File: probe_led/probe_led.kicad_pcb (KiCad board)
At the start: 2 copper layers, 60 x 7 mm, 39 parts

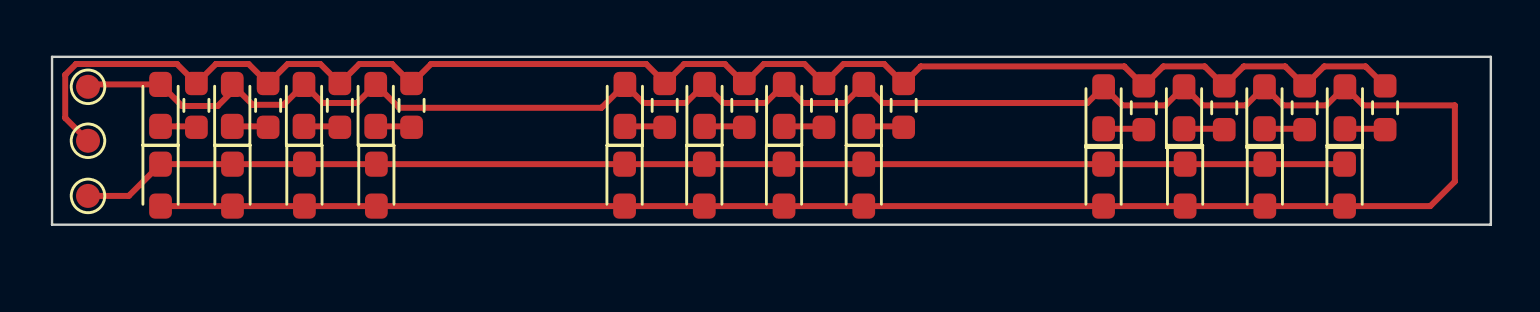
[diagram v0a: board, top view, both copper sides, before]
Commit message: - add led pcb
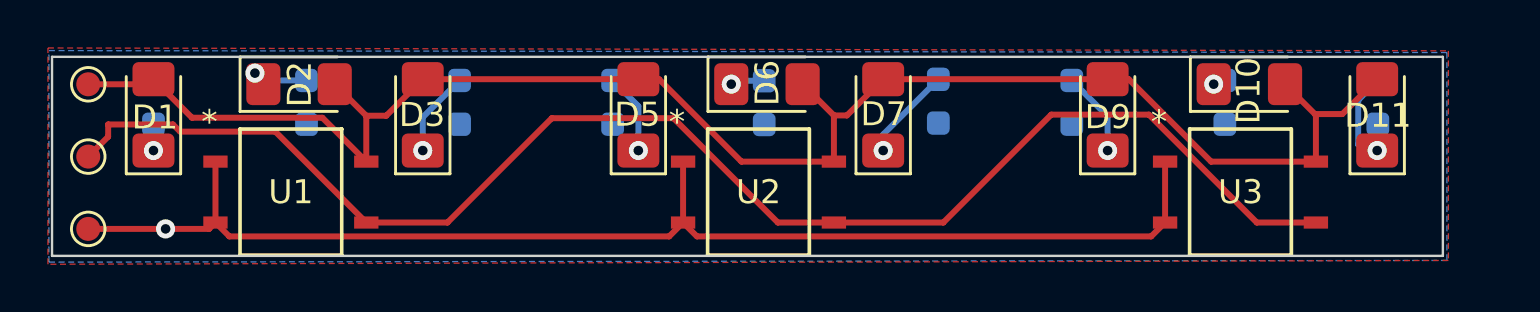
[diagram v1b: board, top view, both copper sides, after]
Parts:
- removed D12, D4, D8, IR10, IR11, IR12, IR2, IR3, IR4, IR5, IR6, IR7, IR8, IR9: LED, LED_SMD:LED_0603_1608Metric_Pad1.05x0.95mm_HandSolder
- removed the IR1 at (104.5, 82.0)
- removed R12, R4, R8: R, Resistor_SMD:R_0603_1608Metric_Pad0.98x0.95mm_HandSolder
- added U1: IRM-H638T_TR2, IRM-H638T:IRM-H638T&slash_TR2_EVE-L, F.Cu at (110.0, 82.3)
- added U2: IRM-H638T_TR2, IRM-H638T:IRM-H638T&slash_TR2_EVE-L, F.Cu at (129.5, 82.3)
- added U3: IRM-H638T_TR2, IRM-H638T:IRM-H638T&slash_TR2_EVE-L, F.Cu at (149.6, 82.3)
- D1, D10, D11, D2, D3, D5, D6, D7, D9: footprint LED_SMD:LED_0603_1608Metric_Pad1.05x0.95mm_HandSolder -> LED_SMD:LED_1206_3216Metric_Pad1.42x1.75mm_HandSolder
- R1, R10, R11, R2, R3, R5, R6, R7, R9: moved to B.Cu
- moved R3 4.99 mm to (117.0, 78.6), turned to -90 degrees
- moved D3 4.97 mm to (115.5, 79.1)
- moved R7 4.77 mm to (137.0, 78.5), turned to -90 degrees
- moved D11 4.71 mm to (155.3, 79.1)
- moved D7 4.15 mm to (134.7, 79.1)
- moved GND1 3.68 mm to (101.5, 83.9)
- moved R11 3.06 mm to (155.3, 78.6), turned to -90 degrees
- moved R9 3.01 mm to (142.5, 78.6), turned to -90 degrees
- moved D2 2.92 mm to (110.3, 77.8), turned to 0 degrees
- moved D10 2.90 mm to (149.9, 77.8), turned to 0 degrees
- moved D6 2.75 mm to (129.8, 77.8), turned to 0 degrees
- moved R5 2.17 mm to (123.4, 78.6), turned to -90 degrees
- moved R1 1.79 mm to (104.2, 78.6)
- moved IR1 1.64 mm to (101.5, 80.9)
- moved R2 1.61 mm to (110.6, 78.6), turned to -90 degrees
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- renumbered 5V to 5V1, GND to GND1, IR to IR1
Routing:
- net +5V: track 122.7 -> 71.3 mm
- net GND: track 66.1 -> 53.6 mm, vias 0 -> 1
- net Net-(IR1-Pad1): track 52.9 -> 61.1 mm
- net Net-(D11-Pad1): track 1.69 -> 4.12 mm, vias 0 -> 1
- net Net-(D7-Pad1): track 1.68 -> 3.92 mm, vias 0 -> 1
- net Net-(D3-Pad1): track 1.51 -> 3.56 mm, vias 0 -> 1
- net Net-(D9-Pad1): track 1.69 -> 3.54 mm, vias 0 -> 1
- net Net-(D12-Pad1): track 1.69 -> 0.00 mm
- net Net-(D5-Pad1): track 1.68 -> 3.37 mm, vias 0 -> 1
- net Net-(D8-Pad1): track 1.68 -> 0.00 mm
- net Net-(D4-Pad1): track 1.51 -> 0.00 mm
- net Net-(D10-Pad1): track 1.69 -> 0.53 mm, vias 0 -> 1
- net Net-(D2-Pad1): track 1.51 -> 2.28 mm, vias 0 -> 1
- net Net-(D1-Pad1): track 1.51 -> 1.10 mm, vias 0 -> 1
- net Net-(D6-Pad1): track 1.68 -> 1.43 mm, vias 0 -> 1
- added copper zone on F.Cu, net +5V
- added copper zone on B.Cu, net GND
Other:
- board size 60 x 7 mm -> 58 x 8.3 mm

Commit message: - add new power version
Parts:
- removed 5V1: 5V, TestPoint:TestPoint_Pad_D1.0mm
- added 5V: 5V, TestPoint:TestPoint_Pad_D1.0mm, F.Cu at (101.5, 77.7)
- added LED-: GND, TestPoint:TestPoint_Pad_D1.0mm, F.Cu at (101.5, 79.7)
- moved IR_D 0.95 mm to (101.5, 81.8)
- renumbered GND1 to IR-, IR1 to IR_D
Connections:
- net +5V renamed Net-(5V-Pad1)
- IR- pad 1: GND -> Net-(IR--Pad1)
- R1 pad 2: GND -> Net-(LED--Pad1)
- R10 pad 2: GND -> Net-(LED--Pad1)
- R11 pad 2: GND -> Net-(LED--Pad1)
- R2 pad 2: GND -> Net-(LED--Pad1)
- R3 pad 2: GND -> Net-(LED--Pad1)
- R5 pad 2: GND -> Net-(LED--Pad1)
- R6 pad 2: GND -> Net-(LED--Pad1)
- R7 pad 2: GND -> Net-(LED--Pad1)
- R9 pad 2: GND -> Net-(LED--Pad1)
- U1 pad 1: GND -> Net-(IR--Pad1)
- U1 pad 2: GND -> Net-(IR--Pad1)
- U2 pad 1: GND -> Net-(IR--Pad1)
- U2 pad 2: GND -> Net-(IR--Pad1)
- U3 pad 1: GND -> Net-(IR--Pad1)
- U3 pad 2: GND -> Net-(IR--Pad1)
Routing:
- net Net-(LED--Pad1): track 0.00 -> 75.3 mm, vias 0 -> 1
- net Net-(IR--Pad1): track 0.00 -> 53.6 mm
- net GND: track 53.6 -> 0.00 mm, vias 1 -> 0
- added copper zone on B.Cu, net Net-(LED--Pad1)
- removed copper zone on B.Cu, net GND

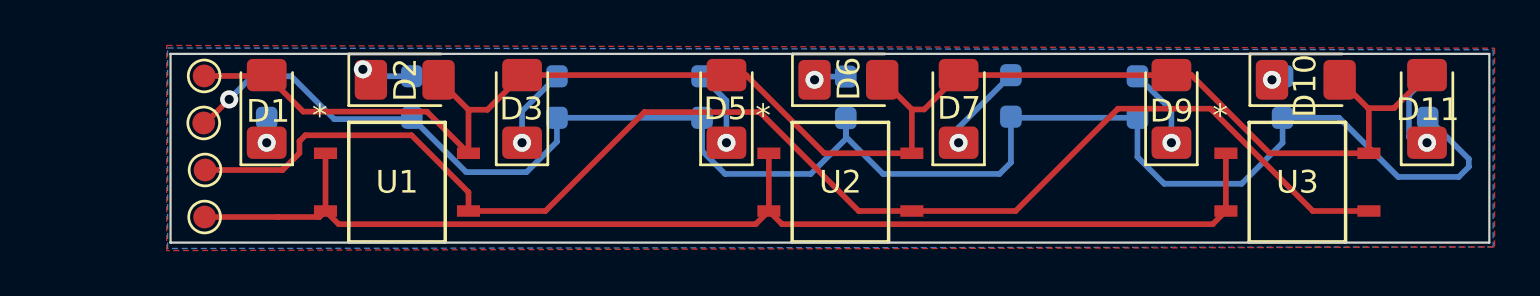
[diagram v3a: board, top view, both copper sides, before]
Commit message: -add new size led
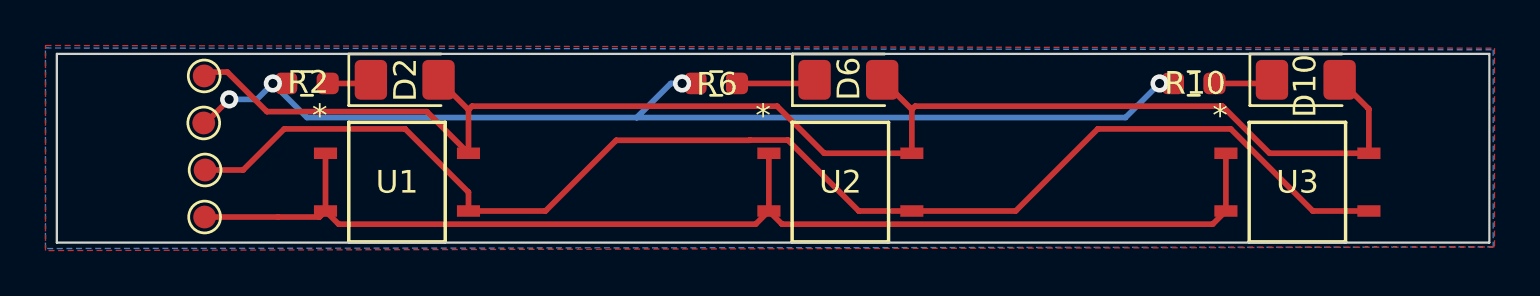
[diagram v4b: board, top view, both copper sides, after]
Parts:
- removed D1, D11, D3, D5, D7, D9: LED, LED_SMD:LED_1206_3216Metric_Pad1.42x1.75mm_HandSolder
- removed R1, R11, R3, R5, R7, R9: R, Resistor_SMD:R_0603_1608Metric_Pad0.98x0.95mm_HandSolder
- R10, R2, R6: moved to F.Cu
- moved R6 5.73 mm to (124.0, 78.0), turned to 180 degrees
- moved R2 4.65 mm to (106.0, 78.0), turned to 180 degrees
- moved R10 3.95 mm to (145.0, 78.0), turned to 180 degrees
- renumbered 5V to 5V1, IR- to IR-1, IR_D to IR_D1, LED- to LED-1
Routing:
- net Net-(LED-1-Pad1): track 75.3 -> 48.4 mm, vias 1 -> 4
- net Net-(D10-A): track 71.6 -> 65.9 mm
- net Net-(D11-Pad1): track 4.12 -> 0.00 mm, vias 1 -> 0
- net Net-(D7-Pad1): track 3.92 -> 0.00 mm, vias 1 -> 0
- net Net-(D3-Pad1): track 3.56 -> 0.00 mm, vias 1 -> 0
- net Net-(D9-Pad1): track 3.54 -> 0.00 mm, vias 1 -> 0
- net Net-(D5-Pad1): track 3.37 -> 0.00 mm, vias 1 -> 0
- net Net-(D10-K): track 0.53 -> 2.60 mm, vias 1 -> 0
- net Net-(D6-K): track 1.43 -> 3.48 mm, vias 1 -> 0
- net Net-(IR_D1-Pad1): track 61.3 -> 59.5 mm
- net Net-(D1-Pad1): track 1.10 -> 0.00 mm, vias 1 -> 0
- net Net-(D2-K): track 2.28 -> 1.97 mm, vias 1 -> 0
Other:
- board size 58 x 8.3 mm -> 63 x 8.3 mm

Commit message: -add new version for transmitter
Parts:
- added REF**: FPC_4pin_0.5mm_fingers, Connector_FFC-FPC:FPC_4pin_0.5mm_fingers, F.Cu at (98.3, 102.5)
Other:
- board size 63 x 8.3 mm -> 60.2 x 68.5 mm
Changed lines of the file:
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@@
 		)
+	)
+	(footprint "Connector_FFC-FPC:FPC_4pin_0.5mm_fingers"
+		(layer "F.Cu")
+		(at 98.3 102.54)
+		(property "Reference" "REF**"
+			(at 0 -4 0)
+			(unlocked yes)
+			(layer "F.SilkS")
+			(effects
+				(font
+					(size 1 1)
+					(thickness 0.15)
+				)
+			)
+		)
+		(property "Value" "FPC_4pin_0.5mm_fingers"
+			(at 0 7 0)
+			(unlocked yes)
+			(layer "F.Fab")
+			(effects
+				(font
+					(size 1 1)
+					(thickness 0.15)
+				)
+			)
+		)
+		(property "Datasheet" ""
+			(at 0 0 0)
+			(unlocked yes)
+			(layer "F.Fab")
+			(hide yes)
+			(effects
+				(font
+					(size 1 1)
+					(thickness 0.15)
+				)
+			)
+		)
+		(property "Description" ""
+			(at 0 0 0)
+			(unlocked yes)
+			(layer "F.Fab")
+			(hide yes)
+			(effects
+				(font
+					(size 1 1)
+					(thickness 0.15)
+				)
+			)
+		)
+		(attr smd)
+		(fp_text user "${REFERENCE}"
+			(at 0 9 0)
+			(unlocked yes)
+			(layer "F.Fab")
+			(effects
+				(font
+					(size 1 1)
+					(thickness 0.15)
+				)
+			)
+		)
+		(pad "1" smd roundrect
+			(at 0 0)
+			(size 0.3 5)
+			(layers "F.Cu" "F.Mask" "F.Paste")
+			(roundrect_rratio 0.15)
+			(thermal_bridge_angle 45)
+			(teardrops
+				(best_length_ratio 0.5)
+				(max_length 1)
+				(best_width_ratio 1)
+				(max_width 2)
+				(curved_edges no)
+				(filter_ratio 0.9)
+				(enabled yes)
+				(allow_two_segments yes)
+				(prefer_zone_connections yes)
+			)
+		)
+		(pad "2" smd roundrect
+			(at 0.5 0)
+			(size 0.3 5)
+			(layers "F.Cu" "F.Mask" "F.Paste")
+			(roundrect_rratio 0.15)
+			(thermal_bridge_angle 45)
+		)
+		(pad "3" smd roundrect
+			(at 1 0)
+			(size 0.3 5)
+			(layers "F.Cu" "F.Mask" "F.Paste")
+			(roundrect_rratio 0.15)
+			(thermal_bridge_angle 45)
+		)
+		(pad "4" smd roundrect
+			(at 1.5 0)
+			(size 0.3 5)
+			(layers "F.Cu" "F.Mask" "F.Paste")
+			(roundrect_rratio 0.15)
+			(thermal_bridge_angle 45)
+		)
+		(embedded_fonts no)
 	)
 	(footprint "Resistor_SMD:R_0603_1608Metric_Pad0.98x0.95mm_HandSolder"
@@
 		)
 	)
-	(gr_rect
-		(start 95 76.7)
-		(end 158 85)
+	(gr_line
+		(start 100.32 36.61)
+		(end 100.32 76.7)
 		(stroke
 			(width 0.1)
-			(type solid)
-		)
-		(fill no)
+			(type default)
+		)
+		(layer "Edge.Cuts")
+	)
+	(gr_line
+		(start 97.81 36.61)
+		(end 100.32 36.61)
+		(stroke
+			(width 0.1)
+			(type default)
+		)
+		(layer "Edge.Cuts")
+	)
+	(gr_line
+		(start 97.78 76.68)
+		(end 97.81 36.61)
+		(stroke
+			(width 0.1)
+			(type default)
+		)
+		(layer "Edge.Cuts")
+	)
+	(gr_line
+		(start 157.99 84.99)
+		(end 100.3 85.03)
+		(stroke
+			(width 0.1)
+			(type default)
+		)
+		(layer "Edge.Cuts")
+	)
+	(gr_line
+		(start 100.3 85.03)
+		(end 100.25 105.08)
+		(stroke
+			(width 0.1)
+			(type default)
+		)
+		(layer "Edge.Cuts")
+	)
+	(gr_line
+		(start 100.32 76.7)
+		(end 157.99 76.65)
+		(stroke
+			(width 0.1)
+			(type default)
+		)
+		(layer "Edge.Cuts")
+	)
+	(gr_line
+		(start 97.83 105.08)
+		(end 97.78 76.68)
+		(stroke
+			(width 0.1)
+			(type default)
+		)
+		(layer "Edge.Cuts")
+	)
+	(gr_line
+		(start 100.25 105.08)
+		(end 97.83 105.08)
+		(stroke
+			(width 0.1)
+			(type default)
+		)
+		(layer "Edge.Cuts")
+	)
+	(gr_line
+		(start 157.99 76.65)
+		(end 157.99 84.99)
+		(stroke
+			(width 0.1)
+			(type default)
+		)
 		(layer "Edge.Cuts")
 	)
@@
 		(polygon
 			(pts
-				(xy 158.23 76.45) (xy 158.23 85.19) (xy 94.5 85.35) (xy 94.5 76.33)
+				(xy 158.45 34.73) (xy 158.64 107.06) (xy 94.16 107.06) (xy 93.79 34.92)
 			)
 		)
@@
 		(polygon
 			(pts
-				(xy 158.17 76.52) (xy 158.17 85.19) (xy 94.5 85.26) (xy 94.5 76.44)
-			)
-		)
+				(xy 158.17 35.294093) (xy 158.17 106.928595) (xy 94.5 106.998595) (xy 94.5 35.214093)
+			)
+		)

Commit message: -prepare for production
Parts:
- removed REF**: FPC_4pin_0.5mm_fingers, Connector_FFC-FPC:FPC_4pin_0.5mm_fingers
- added  : Probe LED v1.4, LOGO, F.Cu at (138.0, 81.0)
- added J3: Conn_01x06, Library:FPC_4pin_0.5mm_fingers, B.Cu at (98.2, 39.2)
- 3V3: renamed from 5V1; value 5V -> 33V
- renumbered LED-1 to IRLED_POW1, IR_D1 to IRREC_DATA1, IR-1 to IRREC_POW1
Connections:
- net Net-(D10-A) renamed +3.3V
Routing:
- net Net-(J3-Pin_3): track 53.6 -> 101.3 mm, vias 0 -> 1
- net Net-(J3-Pin_4): track 59.5 -> 104.0 mm, vias 0 -> 1
- net Net-(J3-Pin_2): track 48.4 -> 91.3 mm, vias 4 -> 5
- net +3.3V: track 65.9 -> 107.1 mm, vias 0 -> 1
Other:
- board size 60.2 x 68.5 mm -> 60.2 x 48.4 mm
